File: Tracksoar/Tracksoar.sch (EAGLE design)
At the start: 35 parts, among them IC2 74AHC1G125DBV, U1 ATMEGA328P, Y1 16MHZ

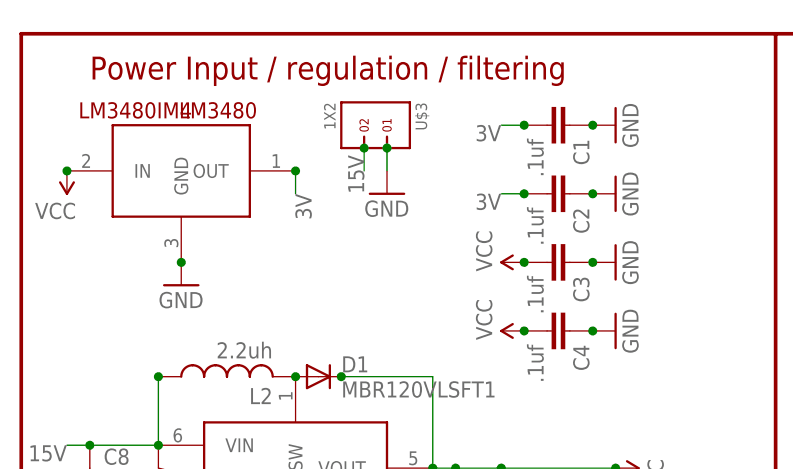
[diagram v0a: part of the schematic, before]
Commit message: Added V1.1 board layout
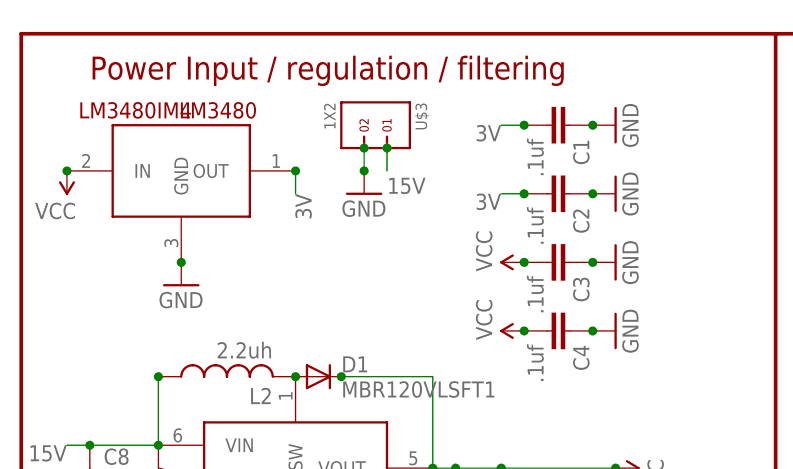
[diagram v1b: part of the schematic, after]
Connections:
- net 15V: now also U$3.1; no longer U$3.2
- net GND: now also U$3.2; no longer U$3.1
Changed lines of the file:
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@@
 <part name="J$1" library="SparkFun-Connectors" deviceset="SMA_EDGE" device=""/>
 <part name="GND4" library="SparkFun-Aesthetics" deviceset="GND" device=""/>
-<part name="GND5" library="SparkFun-Aesthetics" deviceset="GND" device=""/>
 <part name="SUPPLY2" library="SparkFun-Aesthetics" deviceset="VCC" device=""/>
 <part name="SUPPLY3" library="SparkFun-Aesthetics" deviceset="VCC" device=""/>
@@
 <part name="SERIAL" library="headers(2mm)" deviceset="1X4" device=""/>
 <part name="U$3" library="headers(2mm)" deviceset="1X2" device=""/>
+<part name="GND5" library="SparkFun-Aesthetics" deviceset="GND" device=""/>
 </parts>
 <sheets>
@@
 <instance part="J$1" gate="1" x="96.52" y="170.18"/>
 <instance part="GND4" gate="1" x="93.98" y="154.94"/>
-<instance part="GND5" gate="1" x="40.64" y="167.64"/>
 <instance part="SUPPLY2" gate="G$1" x="5.08" y="170.18" rot="R180"/>
 <instance part="SUPPLY3" gate="G$1" x="109.22" y="132.08" rot="R90"/>
@@
 <instance part="SERIAL" gate="G$1" x="228.6" y="86.36"/>
 <instance part="U$3" gate="G$1" x="40.64" y="175.26" rot="R270"/>
+<instance part="GND5" gate="1" x="38.1" y="167.64"/>
 </instances>
 <busses>
@@
 </segment>
 <segment>
-<pinref part="GND5" gate="1" pin="GND"/>
-<pinref part="U$3" gate="G$1" pin="1"/>
-<wire x1="40.64" y1="172.72" x2="40.64" y2="170.18" width="0.1524" layer="91"/>
-<junction x="40.64" y="172.72"/>
-</segment>
-<segment>
 <pinref part="U$2" gate="G$1" pin="0V"/>
 <pinref part="GND7" gate="1" pin="GND"/>
@@
 <pinref part="GND20" gate="1" pin="GND"/>
 <junction x="104.14" y="73.66"/>
+</segment>
+<segment>
+<pinref part="U$3" gate="G$1" pin="2"/>
+<wire x1="38.1" y1="172.72" x2="38.1" y2="170.18" width="0.1524" layer="91"/>
+<junction x="38.1" y="172.72"/>
+<pinref part="GND5" gate="1" pin="GND"/>
+<junction x="38.1" y="170.18"/>
 </segment>
 </net>
@@
 </segment>
 <segment>
-<label x="38.1" y="167.64" size="1.778" layer="95" rot="R90"/>
-<pinref part="U$3" gate="G$1" pin="2"/>
-<wire x1="38.1" y1="172.72" x2="38.1" y2="170.18" width="0.1524" layer="91"/>
-<junction x="38.1" y="172.72"/>
-</segment>
-</net>
+<pinref part="U$3" gate="G$1" pin="1"/>
+<wire x1="40.64" y1="172.72" x2="40.64" y2="170.18" width="0.1524" layer="91"/>
+<junction x="40.64" y="172.72"/>
+<label x="40.64" y="167.64" size="1.778" layer="95"/>
+</segment>
+</net>

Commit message: Added V1.2 board
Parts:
- removed BMP180: BMP180, SparkFun-Sensors:BMP180
- removed SHT21: SHT21, sht21:SHT21
- added IC1: BME280, bosch-bme280:BME280
- added R2: 4.7k, SparkFun-Resistors:RESISTOR0805-RES
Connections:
- new net N$2: IC1.CSB, R2.2
- net 3V: now also IC1.VDD, IC1.VDDIO, R2.1; no longer BMP180.VDD, BMP180.VDDIO, SHT21.VDD
- net GND: now also IC1.GND, IC1.SDO; no longer BMP180.GND, SHT21.VSS
- net SCL: now also IC1.SCK; no longer BMP180.SCL, SHT21.SCL
- net SDA: now also IC1.SDI; no longer BMP180.SDA, SHT21.SDA
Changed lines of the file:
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@@
 <part name="GND3" library="SparkFun-Aesthetics" deviceset="GND" device=""/>
 <part name="GND10" library="SparkFun-Aesthetics" deviceset="GND" device=""/>
-<part name="BMP180" library="SparkFun-Sensors" deviceset="BMP180" device=""/>
-<part name="GND16" library="SparkFun-Aesthetics" deviceset="GND" device=""/>
 <part name="GND20" library="SparkFun-Aesthetics" deviceset="GND" device=""/>
 <part name="R3" library="SparkFun-Resistors" deviceset="RESISTOR" device="0805-RES" value="4.7k"/>
@@
 <part name="GND29" library="SparkFun-Aesthetics" deviceset="GND" device=""/>
 <part name="GND30" library="SparkFun-Aesthetics" deviceset="GND" device=""/>
-<part name="SHT21" library="sht21" deviceset="SHT21" device=""/>
 <part name="GPS-ANT" library="SparkFun-RF" deviceset="ANTENNA2" device="SMD3"/>
 <part name="FTDI" library="headers(2mm)" deviceset="1X7" device=""/>
@@
 <part name="U$3" library="headers(2mm)" deviceset="1X2" device=""/>
 <part name="GND5" library="SparkFun-Aesthetics" deviceset="GND" device=""/>
+<part name="IC1" library="bosch-bme280" deviceset="BME280" device=""/>
+<part name="GND6" library="SparkFun-Aesthetics" deviceset="GND" device=""/>
+<part name="R2" library="SparkFun-Resistors" deviceset="RESISTOR" device="0805-RES" value="4.7k"/>
 </parts>
 <sheets>
@@
 <instance part="GND3" gate="1" x="17.78" y="157.48"/>
 <instance part="GND10" gate="1" x="208.28" y="58.42" rot="R90"/>
-<instance part="BMP180" gate="G$1" x="104.14" y="48.26"/>
-<instance part="GND16" gate="1" x="121.92" y="43.18" rot="R90"/>
-<instance part="GND20" gate="1" x="101.6" y="73.66" rot="R270"/>
+<instance part="GND20" gate="1" x="106.68" y="76.2" rot="R270"/>
 <instance part="R3" gate="G$1" x="129.54" y="48.26" rot="R270"/>
 <instance part="R7" gate="G$1" x="137.16" y="48.26" rot="R270"/>
@@
 <instance part="GND29" gate="1" x="7.62" y="129.54"/>
 <instance part="GND30" gate="1" x="53.34" y="127"/>
-<instance part="SHT21" gate="A" x="121.92" y="83.82"/>
 <instance part="GPS-ANT" gate="G$1" x="165.1" y="165.1" rot="R90"/>
 <instance part="FTDI" gate="G$1" x="200.66" y="53.34"/>
@@
 <instance part="U$3" gate="G$1" x="40.64" y="175.26" rot="R270"/>
 <instance part="GND5" gate="1" x="38.1" y="167.64"/>
+<instance part="IC1" gate="G$1" x="121.92" y="81.28"/>
+<instance part="GND6" gate="1" x="137.16" y="73.66"/>
+<instance part="R2" gate="G$1" x="104.14" y="81.28"/>
 </instances>
 <busses>
@@
 </segment>
 <segment>
-<pinref part="BMP180" gate="G$1" pin="GND"/>
-<pinref part="GND16" gate="1" pin="GND"/>
-<junction x="119.38" y="43.18"/>
-</segment>
-<segment>
 <pinref part="LT3426" gate="G$1" pin="GND"/>
 <pinref part="GND27" gate="1" pin="GND"/>
@@
 <pinref part="GND30" gate="1" pin="GND"/>
 <junction x="53.34" y="129.54"/>
-</segment>
-<segment>
-<pinref part="SHT21" gate="A" pin="VSS"/>
-<pinref part="GND20" gate="1" pin="GND"/>
-<junction x="104.14" y="73.66"/>
 </segment>
 <segment>
@@
 <pinref part="GND5" gate="1" pin="GND"/>
 <junction x="38.1" y="170.18"/>
+</segment>
+<segment>
+<pinref part="IC1" gate="G$1" pin="GND"/>
+<pinref part="GND20" gate="1" pin="GND"/>
+<junction x="109.22" y="76.2"/>
+</segment>
+<segment>
+<pinref part="IC1" gate="G$1" pin="SDO"/>
+<pinref part="GND6" gate="1" pin="GND"/>
+<wire x1="137.16" y1="76.2" x2="134.62" y2="76.2" width="0.1524" layer="91"/>
+<junction x="134.62" y="76.2"/>
+<junction x="137.16" y="76.2"/>
 </segment>
 </net>
@@
 </segment>
 <segment>
-<pinref part="BMP180" gate="G$1" pin="VDD"/>
-<pinref part="BMP180" gate="G$1" pin="VDDIO"/>
-<wire x1="119.38" y1="53.34" x2="119.38" y2="50.8" width="0.1524" layer="91"/>
-<wire x1="119.38" y1="50.8" x2="119.38" y2="48.26" width="0.1524" layer="91"/>
-<wire x1="119.38" y1="50.8" x2="121.92" y2="50.8" width="0.1524" layer="91"/>
-<junction x="119.38" y="53.34"/>
-<junction x="119.38" y="48.26"/>
-<junction x="119.38" y="50.8"/>
-<label x="121.92" y="50.8" size="1.778" layer="95"/>
-</segment>
-<segment>
-<wire x1="104.14" y1="91.44" x2="101.6" y2="91.44" width="0.1524" layer="91"/>
-<label x="101.6" y="91.44" size="1.778" layer="95"/>
-<pinref part="SHT21" gate="A" pin="VDD"/>
-<junction x="104.14" y="91.44"/>
+<wire x1="109.22" y1="86.36" x2="106.68" y2="86.36" width="0.1524" layer="91"/>
+<label x="104.14" y="86.36" size="1.778" layer="95"/>
+<label x="137.16" y="83.82" size="1.778" layer="95"/>
+<label x="93.98" y="81.28" size="1.778" layer="95"/>
+<pinref part="IC1" gate="G$1" pin="VDD"/>
+<junction x="109.22" y="86.36"/>
 </segment>
 <segment>
@@
 <junction x="137.16" y="53.34"/>
 </segment>
+<segment>
+<wire x1="137.16" y1="83.82" x2="134.62" y2="83.82" width="0.1524" layer="91"/>
+<pinref part="IC1" gate="G$1" pin="VDDIO"/>
+<junction x="134.62" y="83.82"/>
+</segment>
+<segment>
+<wire x1="99.06" y1="81.28" x2="96.52" y2="81.28" width="0.1524" layer="91"/>
+<pinref part="R2" gate="G$1" pin="1"/>
+<junction x="99.06" y="81.28"/>
+</segment>
 </net>
 <net name="N$1" class="0">
@@
 </segment>
 <segment>
-<wire x1="142.24" y1="91.44" x2="139.7" y2="91.44" width="0.1524" layer="91"/>
-<label x="139.7" y="91.44" size="1.778" layer="95"/>
-<pinref part="SHT21" gate="A" pin="SDA"/>
-<junction x="139.7" y="91.44"/>
-</segment>
-<segment>
-<pinref part="BMP180" gate="G$1" pin="SDA"/>
-<wire x1="88.9" y1="50.8" x2="86.36" y2="50.8" width="0.1524" layer="91"/>
-<label x="86.36" y="50.8" size="1.778" layer="95"/>
-<junction x="88.9" y="50.8"/>
+<wire x1="137.16" y1="78.74" x2="134.62" y2="78.74" width="0.1524" layer="91"/>
+<label x="137.16" y="78.74" size="1.778" layer="95"/>
+<pinref part="IC1" gate="G$1" pin="SDI"/>
+<junction x="134.62" y="78.74"/>
 </segment>
 <segment>
@@
 </segment>
 <segment>
-<wire x1="104.14" y1="86.36" x2="101.6" y2="86.36" width="0.1524" layer="91"/>
-<label x="101.6" y="86.36" size="1.778" layer="95"/>
-<pinref part="SHT21" gate="A" pin="SCL"/>
-<junction x="104.14" y="86.36"/>
-</segment>
-<segment>
-<pinref part="BMP180" gate="G$1" pin="SCL"/>
-<wire x1="88.9" y1="45.72" x2="86.36" y2="45.72" width="0.1524" layer="91"/>
-<label x="86.36" y="45.72" size="1.778" layer="95"/>
-<junction x="88.9" y="45.72"/>
+<wire x1="137.16" y1="81.28" x2="134.62" y2="81.28" width="0.1524" layer="91"/>
+<label x="137.16" y="81.28" size="1.778" layer="95"/>
+<pinref part="IC1" gate="G$1" pin="SCK"/>
+<junction x="134.62" y="81.28"/>
 </segment>
 <segment>
@@
 </segment>
 </net>
+<net name="N$2" class="0">
+<segment>
+<pinref part="IC1" gate="G$1" pin="CSB"/>
+<pinref part="R2" gate="G$1" pin="2"/>
+<junction x="109.22" y="81.28"/>
+</segment>
+</net>
 </nets>
 </sheet>
@@
 </schematic>
 </drawing>
+<compatibility>
+<note version="6.3" minversion="6.2.2" severity="warning">
+Since Version 6.2.2 text objects can contain more than one line,
+which will not be processed correctly with this version.
+</note>
+</compatibility>
 </eagle>

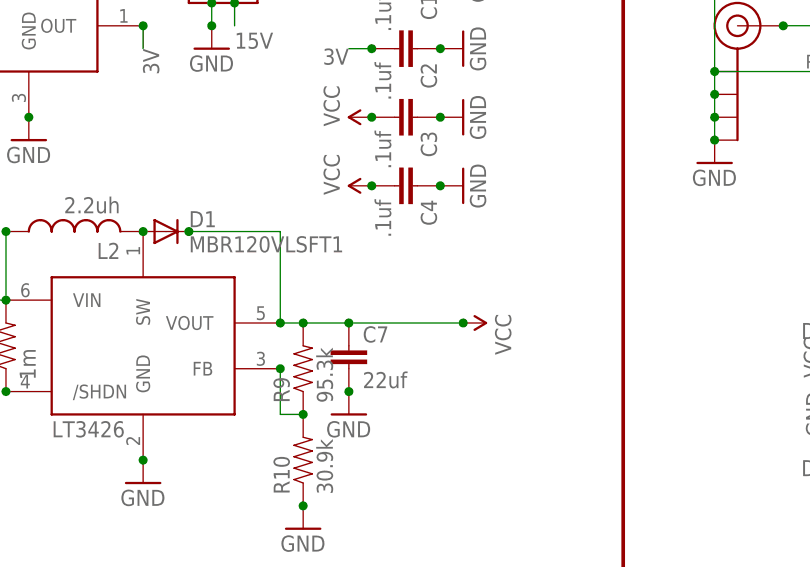
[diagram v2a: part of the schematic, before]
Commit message: BME280 Decoupling Cap
Added a 100nf decoupling cap next to the bme280
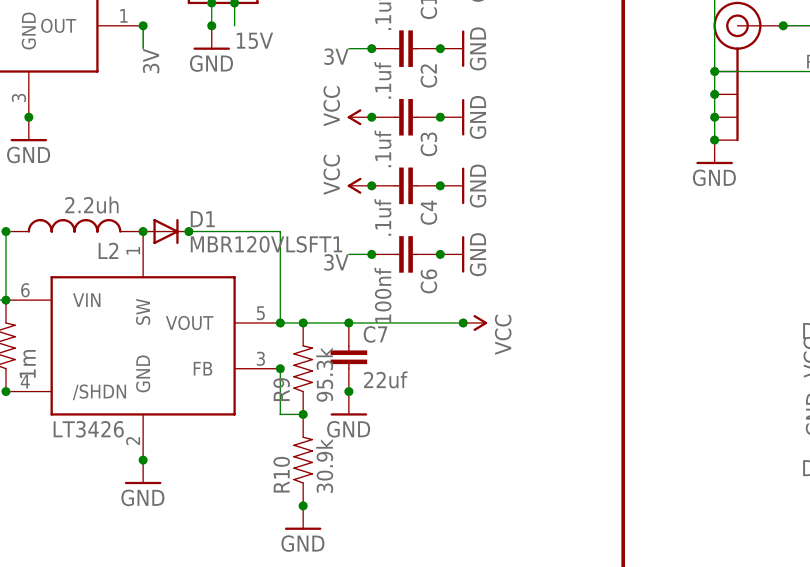
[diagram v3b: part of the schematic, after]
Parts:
- added C6: 100nf, SparkFun-Capacitors:CAP0805
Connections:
- net 3V: now also C6.2
- net GND: now also C6.1
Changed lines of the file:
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@@
 <?xml version="1.0" encoding="utf-8"?>
 <!DOCTYPE eagle SYSTEM "eagle.dtd">
-<eagle version="7.3.0">
+<eagle version="7.5.0">
 <drawing>
 <settings>
@@
 <part name="GND6" library="SparkFun-Aesthetics" deviceset="GND" device=""/>
 <part name="R2" library="SparkFun-Resistors" deviceset="RESISTOR" device="0805-RES" value="4.7k"/>
+<part name="C6" library="SparkFun-Capacitors" deviceset="CAP" device="0805" value="100nf"/>
+<part name="GND11" library="SparkFun-Aesthetics" deviceset="GND" device=""/>
 </parts>
 <sheets>
@@
 <instance part="GND6" gate="1" x="137.16" y="73.66"/>
 <instance part="R2" gate="G$1" x="104.14" y="81.28"/>
+<instance part="C6" gate="G$1" x="58.42" y="144.78" rot="R270"/>
+<instance part="GND11" gate="1" x="66.04" y="144.78" rot="R90"/>
 </instances>
 <busses>
@@
 <junction x="137.16" y="76.2"/>
 </segment>
+<segment>
+<pinref part="C6" gate="G$1" pin="1"/>
+<pinref part="GND11" gate="1" pin="GND"/>
+<junction x="63.5" y="144.78"/>
+</segment>
 </net>
 <net name="D3" class="0">
@@
 <junction x="99.06" y="81.28"/>
 </segment>
+<segment>
+<pinref part="C6" gate="G$1" pin="2"/>
+<wire x1="55.88" y1="144.78" x2="53.34" y2="144.78" width="0.1524" layer="91"/>
+<label x="53.34" y="144.78" size="1.778" layer="95" rot="R180"/>
+<junction x="55.88" y="144.78"/>
+</segment>
 </net>
